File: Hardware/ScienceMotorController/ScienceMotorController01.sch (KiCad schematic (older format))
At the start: 9 parts

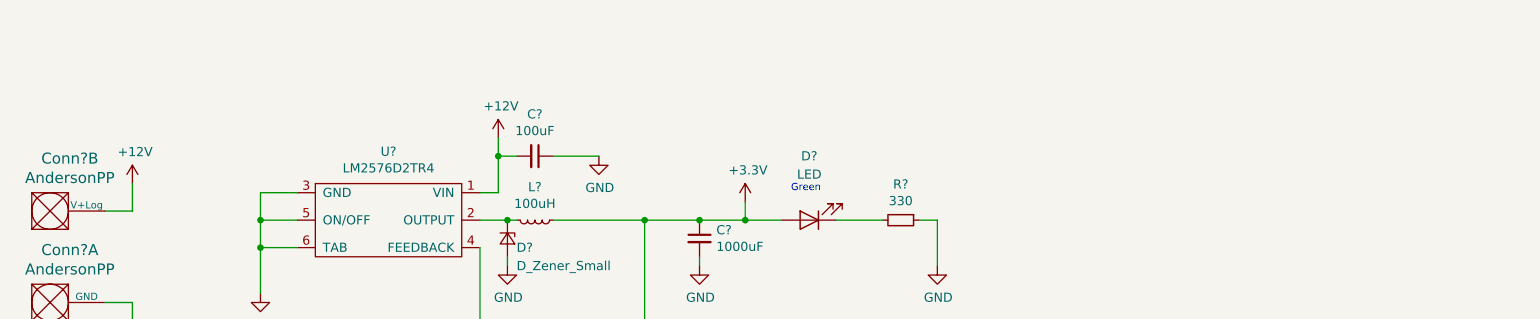
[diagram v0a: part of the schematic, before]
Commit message: Added 12VA anderson
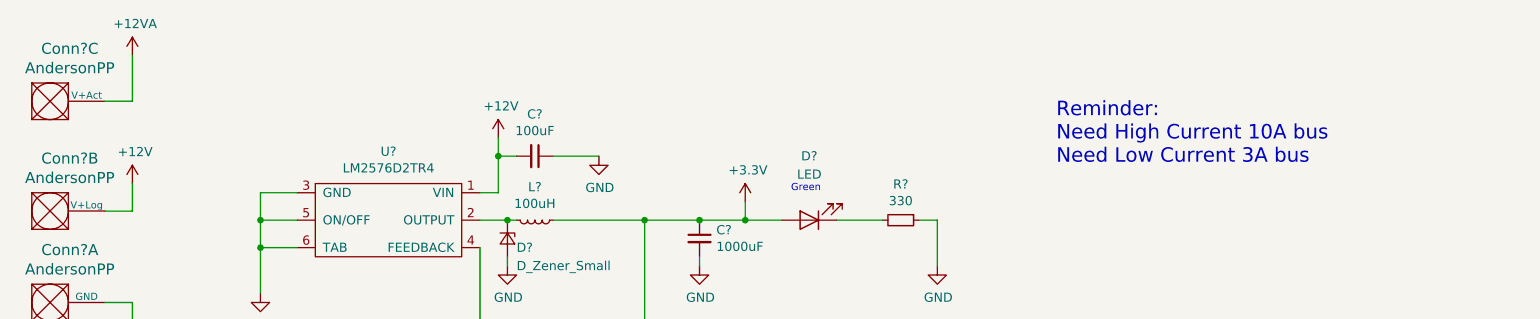
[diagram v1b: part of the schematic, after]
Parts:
- added Conn?: AndersonPP, symbol MRDT_Connectors:AndersonPP
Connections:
- new net +12VA: Conn?.3 (V+Act)
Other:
- note added: "Reminder:\nNeed High Current 10A bus\nNeed Low Current 3A bus"
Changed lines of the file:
@@
 Wire Wire Line
 	6450 1900 6450 2150
+Text Notes 7100 1600 0    79   ~ 0
+Reminder:\nNeed High Current 10A bus\nNeed Low Current 3A bus
+$Comp
+L MRDT_Connectors:AndersonPP Conn?
+U 3 1 5F759AF7
+P 1500 1350
+F 0 "Conn?" H 1708 1737 60  0000 C CNN
+F 1 "AndersonPP" H 1708 1631 60  0000 C CNN
+F 2 "" H 1350 800 60  0001 C CNN
+F 3 "" H 1350 800 60  0001 C CNN
+	3    1500 1350
+	1    0    0    -1
+$EndComp
+Wire Wire Line
+	1900 1250 2050 1250
+Wire Wire Line
+	2050 1250 2050 1000
+$Comp
+L power:+12VA #PWR?
+U 1 1 5F75C024
+P 2050 1000
+F 0 "#PWR?" H 2050 850 50  0001 C CNN
+F 1 "+12VA" H 2065 1173 50  0000 C CNN
+F 2 "" H 2050 1000 50  0001 C CNN
+F 3 "" H 2050 1000 50  0001 C CNN
+	1    2050 1000
+	1    0    0    -1
+$EndComp
 $EndSCHEMATC

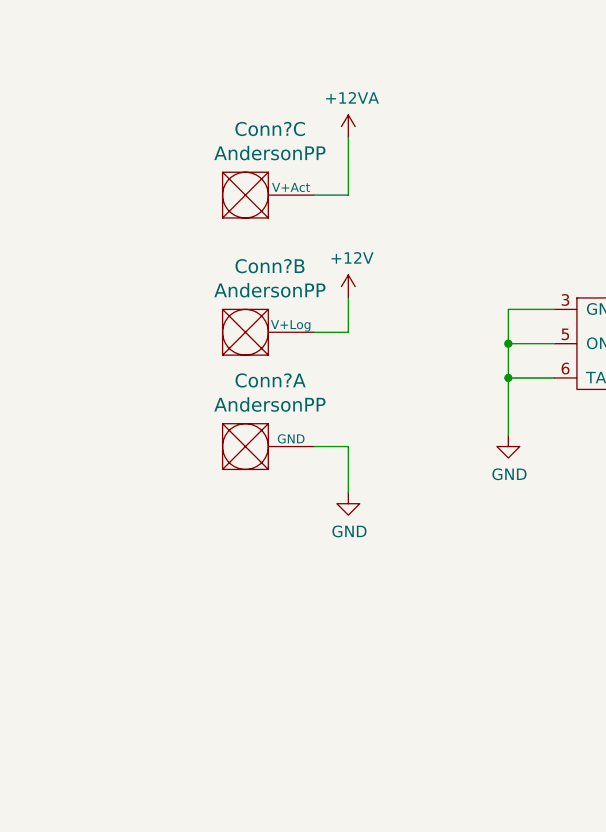
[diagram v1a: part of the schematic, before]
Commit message: power indicators
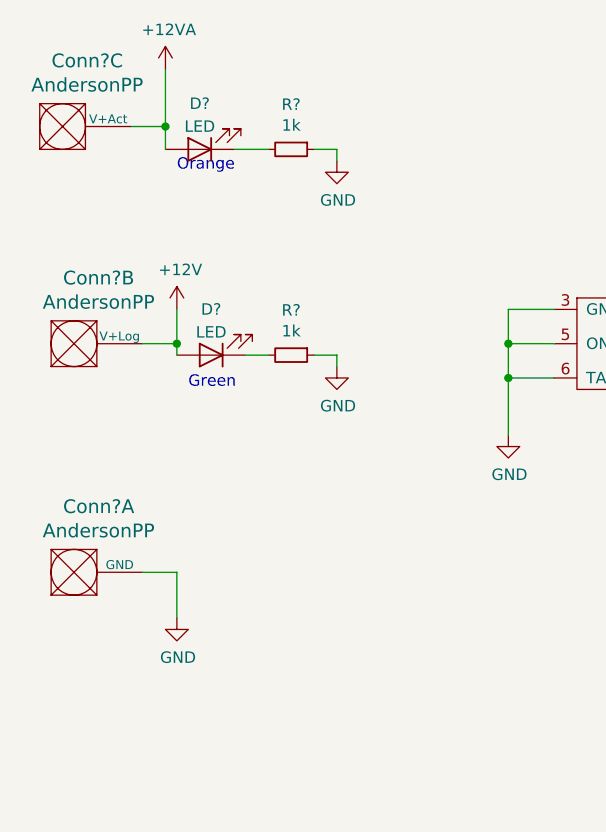
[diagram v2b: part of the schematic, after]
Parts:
- added D? (x2): LED, symbol Device:LED
- added R? (x2): 1k, symbol Device:R_Small
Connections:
- net +12V: now also D?.2 (A)
- net +12VA: now also D?.2 (A)
- net GND: now also R?.1, R?.1
- new net: D?.1 (K), R?.2 (x2)
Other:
- note added: "Orange"
- moved on the sheet: Conn?A, Conn?B, Conn?C
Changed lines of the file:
@@
 L MRDT_Connectors:AndersonPP Conn?
 U 2 1 5F6E2CCA
-P 1500 1950
-F 0 "Conn?" H 1708 2337 60  0000 C CNN
-F 1 "AndersonPP" H 1708 2231 60  0000 C CNN
-F 2 "" H 1350 1400 60  0001 C CNN
-F 3 "" H 1350 1400 60  0001 C CNN
-	2    1500 1950
+P 750 2000
+F 0 "Conn?" H 958 2387 60  0000 C CNN
+F 1 "AndersonPP" H 958 2281 60  0000 C CNN
+F 2 "" H 600 1450 60  0001 C CNN
+F 3 "" H 600 1450 60  0001 C CNN
+	2    750  2000
 	1    0    0    -1
 $EndComp
@@
 L MRDT_Connectors:AndersonPP Conn?
 U 1 1 5F6E39B8
-P 1500 2450
-F 0 "Conn?" H 1708 2837 60  0000 C CNN
-F 1 "AndersonPP" H 1708 2731 60  0000 C CNN
-F 2 "" H 1350 1900 60  0001 C CNN
-F 3 "" H 1350 1900 60  0001 C CNN
-	1    1500 2450
+P 750 3000
+F 0 "Conn?" H 958 3387 60  0000 C CNN
+F 1 "AndersonPP" H 958 3281 60  0000 C CNN
+F 2 "" H 600 2450 60  0001 C CNN
+F 3 "" H 600 2450 60  0001 C CNN
+	1    750  3000
 	1    0    0    -1
 $EndComp
@@
 L power:GND #PWR?
 U 1 1 5F6E83C1
-P 2050 2550
-F 0 "#PWR?" H 2050 2300 50  0001 C CNN
-F 1 "GND" H 2055 2377 50  0000 C CNN
-F 2 "" H 2050 2550 50  0001 C CNN
-F 3 "" H 2050 2550 50  0001 C CNN
-	1    2050 2550
+P 1300 3100
+F 0 "#PWR?" H 1300 2850 50  0001 C CNN
+F 1 "GND" H 1305 2927 50  0000 C CNN
+F 2 "" H 1300 3100 50  0001 C CNN
+F 3 "" H 1300 3100 50  0001 C CNN
+	1    1300 3100
 	1    0    0    -1
 $EndComp
@@
 L power:+12V #PWR?
 U 1 1 5F6E992B
-P 2050 1700
-F 0 "#PWR?" H 2050 1550 50  0001 C CNN
-F 1 "+12V" H 2065 1873 50  0000 C CNN
-F 2 "" H 2050 1700 50  0001 C CNN
-F 3 "" H 2050 1700 50  0001 C CNN
-	1    2050 1700
-	1    0    0    -1
-$EndComp
-Wire Wire Line
-	1900 1850 2050 1850
-Wire Wire Line
-	2050 1850 2050 1700
-Wire Wire Line
-	2050 2550 2050 2350
-Wire Wire Line
-	2050 2350 1900 2350
+P 1300 1750
+F 0 "#PWR?" H 1300 1600 50  0001 C CNN
+F 1 "+12V" H 1315 1923 50  0000 C CNN
+F 2 "" H 1300 1750 50  0001 C CNN
+F 3 "" H 1300 1750 50  0001 C CNN
+	1    1300 1750
+	1    0    0    -1
+$EndComp
+Wire Wire Line
+	1150 1900 1300 1900
+Wire Wire Line
+	1300 3100 1300 2900
+Wire Wire Line
+	1300 2900 1150 2900
 Wire Wire Line
 	2950 1750 2750 1750
@@
 L MRDT_Connectors:AndersonPP Conn?
 U 3 1 5F759AF7
-P 1500 1350
-F 0 "Conn?" H 1708 1737 60  0000 C CNN
-F 1 "AndersonPP" H 1708 1631 60  0000 C CNN
-F 2 "" H 1350 800 60  0001 C CNN
-F 3 "" H 1350 800 60  0001 C CNN
-	3    1500 1350
-	1    0    0    -1
-$EndComp
-Wire Wire Line
-	1900 1250 2050 1250
-Wire Wire Line
-	2050 1250 2050 1000
+P 700 1050
+F 0 "Conn?" H 908 1437 60  0000 C CNN
+F 1 "AndersonPP" H 908 1331 60  0000 C CNN
+F 2 "" H 550 500 60  0001 C CNN
+F 3 "" H 550 500 60  0001 C CNN
+	3    700  1050
+	1    0    0    -1
+$EndComp
+Wire Wire Line
+	1100 950  1250 950
+Wire Wire Line
+	1250 950  1250 700
 $Comp
 L power:+12VA #PWR?
 U 1 1 5F75C024
-P 2050 1000
-F 0 "#PWR?" H 2050 850 50  0001 C CNN
-F 1 "+12VA" H 2065 1173 50  0000 C CNN
-F 2 "" H 2050 1000 50  0001 C CNN
-F 3 "" H 2050 1000 50  0001 C CNN
-	1    2050 1000
-	1    0    0    -1
-$EndComp
+P 1250 700
+F 0 "#PWR?" H 1250 550 50  0001 C CNN
+F 1 "+12VA" H 1265 873 50  0000 C CNN
+F 2 "" H 1250 700 50  0001 C CNN
+F 3 "" H 1250 700 50  0001 C CNN
+	1    1250 700
+	1    0    0    -1
+$EndComp
+$Comp
+L Device:LED D?
+U 1 1 5F7BA809
+P 1400 1050
+F 0 "D?" H 1400 850 50  0000 C CNN
+F 1 "LED" H 1400 950 50  0000 C CNN
+F 2 "" H 1400 1050 50  0001 C CNN
+F 3 "~" H 1400 1050 50  0001 C CNN
+	1    1400 1050
+	-1   0    0    1
+$EndComp
+Wire Wire Line
+	1250 1050 1250 950
+Connection ~ 1250 950
+$Comp
+L Device:R_Small R?
+U 1 1 5F7BD886
+P 1800 1050
+F 0 "R?" V 1604 1050 50  0000 C CNN
+F 1 "1k" V 1695 1050 50  0000 C CNN
+F 2 "" H 1800 1050 50  0001 C CNN
+F 3 "~" H 1800 1050 50  0001 C CNN
+	1    1800 1050
+	0    1    1    0
+$EndComp
+Wire Wire Line
+	1550 1050 1700 1050
+$Comp
+L power:GND #PWR?
+U 1 1 5F7BF549
+P 2000 1100
+F 0 "#PWR?" H 2000 850 50  0001 C CNN
+F 1 "GND" H 2005 927 50  0000 C CNN
+F 2 "" H 2000 1100 50  0001 C CNN
+F 3 "" H 2000 1100 50  0001 C CNN
+	1    2000 1100
+	1    0    0    -1
+$EndComp
+Wire Wire Line
+	1900 1050 2000 1050
+Wire Wire Line
+	2000 1050 2000 1100
+Text Notes 1300 1150 0    50   ~ 0
+Orange
+$Comp
+L Device:LED D?
+U 1 1 5F7C0921
+P 1450 1950
+F 0 "D?" H 1450 1750 50  0000 C CNN
+F 1 "LED" H 1450 1850 50  0000 C CNN
+F 2 "" H 1450 1950 50  0001 C CNN
+F 3 "~" H 1450 1950 50  0001 C CNN
+	1    1450 1950
+	-1   0    0    1
+$EndComp
+Wire Wire Line
+	1300 1750 1300 1900
+Connection ~ 1300 1900
+Wire Wire Line
+	1300 1900 1300 1950
+$Comp
+L Device:R_Small R?
+U 1 1 5F7CD72E
+P 1800 1950
+F 0 "R?" V 1604 1950 50  0000 C CNN
+F 1 "1k" V 1695 1950 50  0000 C CNN
+F 2 "" H 1800 1950 50  0001 C CNN
+F 3 "~" H 1800 1950 50  0001 C CNN
+	1    1800 1950
+	0    1    1    0
+$EndComp
+Wire Wire Line
+	1700 1950 1600 1950
+$Comp
+L power:GND #PWR?
+U 1 1 5F7CEAC2
+P 2000 2000
+F 0 "#PWR?" H 2000 1750 50  0001 C CNN
+F 1 "GND" H 2005 1827 50  0000 C CNN
+F 2 "" H 2000 2000 50  0001 C CNN
+F 3 "" H 2000 2000 50  0001 C CNN
+	1    2000 2000
+	1    0    0    -1
+$EndComp
+Wire Wire Line
+	1900 1950 2000 1950
+Wire Wire Line
+	2000 1950 2000 2000
+Text Notes 1350 2100 0    50   ~ 0
+Green
 $EndSCHEMATC
